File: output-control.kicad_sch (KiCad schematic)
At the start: 57 parts, among them U18 ADS7828, U19 TCA9534PWR, U20 ADS7828

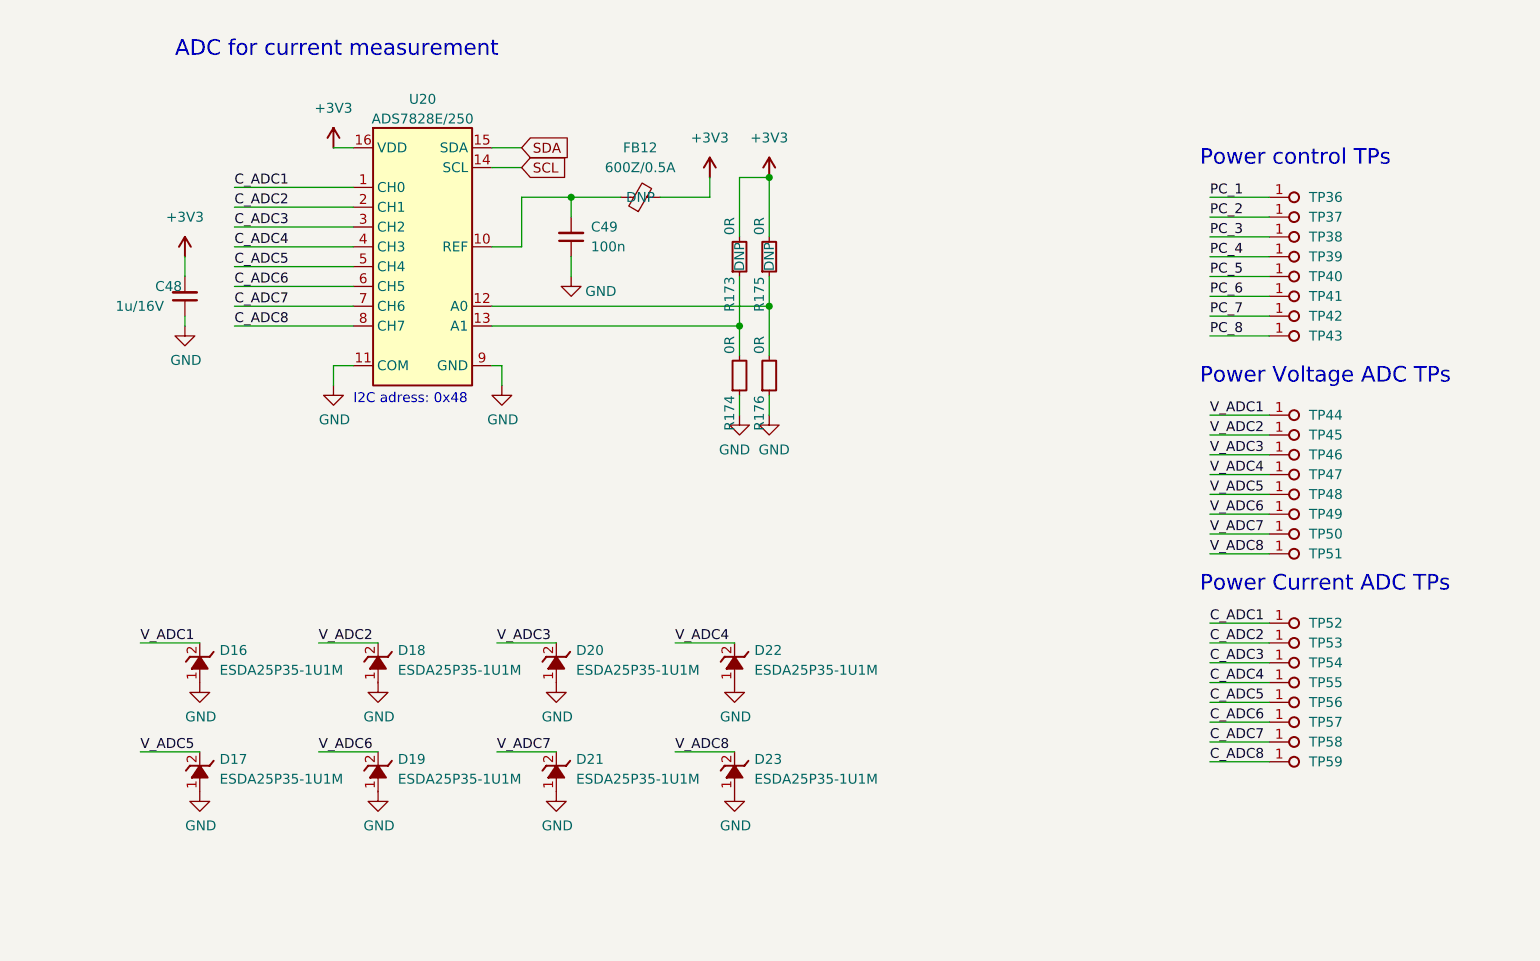
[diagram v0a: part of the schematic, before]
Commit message: Move testpoints to hierarchical sheets
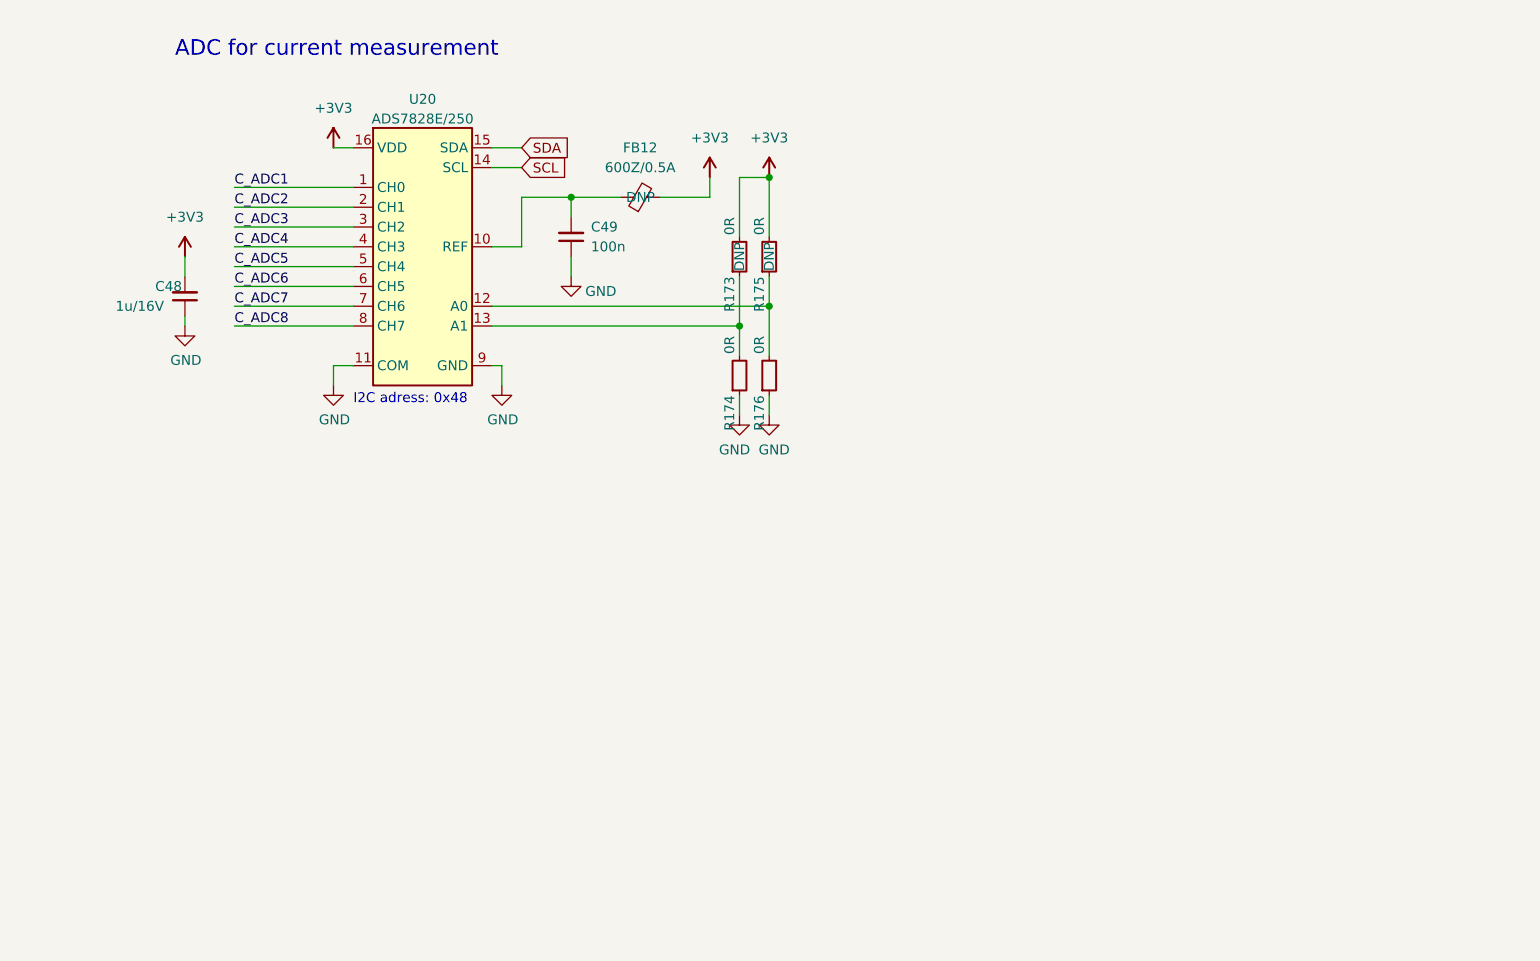
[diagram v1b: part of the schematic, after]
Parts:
- removed D16, D17, D18, D19, D20, D21, D22, D23: ESDA25P35-1U1M, antmicro-footprints:ESDA25P35-1U1M, symbol antmicroTVSDiodes:ESDA25P35-1U1M
- removed TP36, TP37, TP38, TP39, TP40, TP41, TP42, TP43, TP44, TP45, TP46, TP47, TP48, TP49, TP50, TP51, TP52, TP53, TP54, TP55, TP56, TP57, TP58, TP59: TP_1mm_SMD, antmicro-footprints:TP_SMD_1mm, symbol antmicroTestPoints:TP_1mm_SMD
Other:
- note removed: "Power Current ADC TPs"
- note removed: "Power Voltage ADC TPs"
- note removed: "Power control TPs"

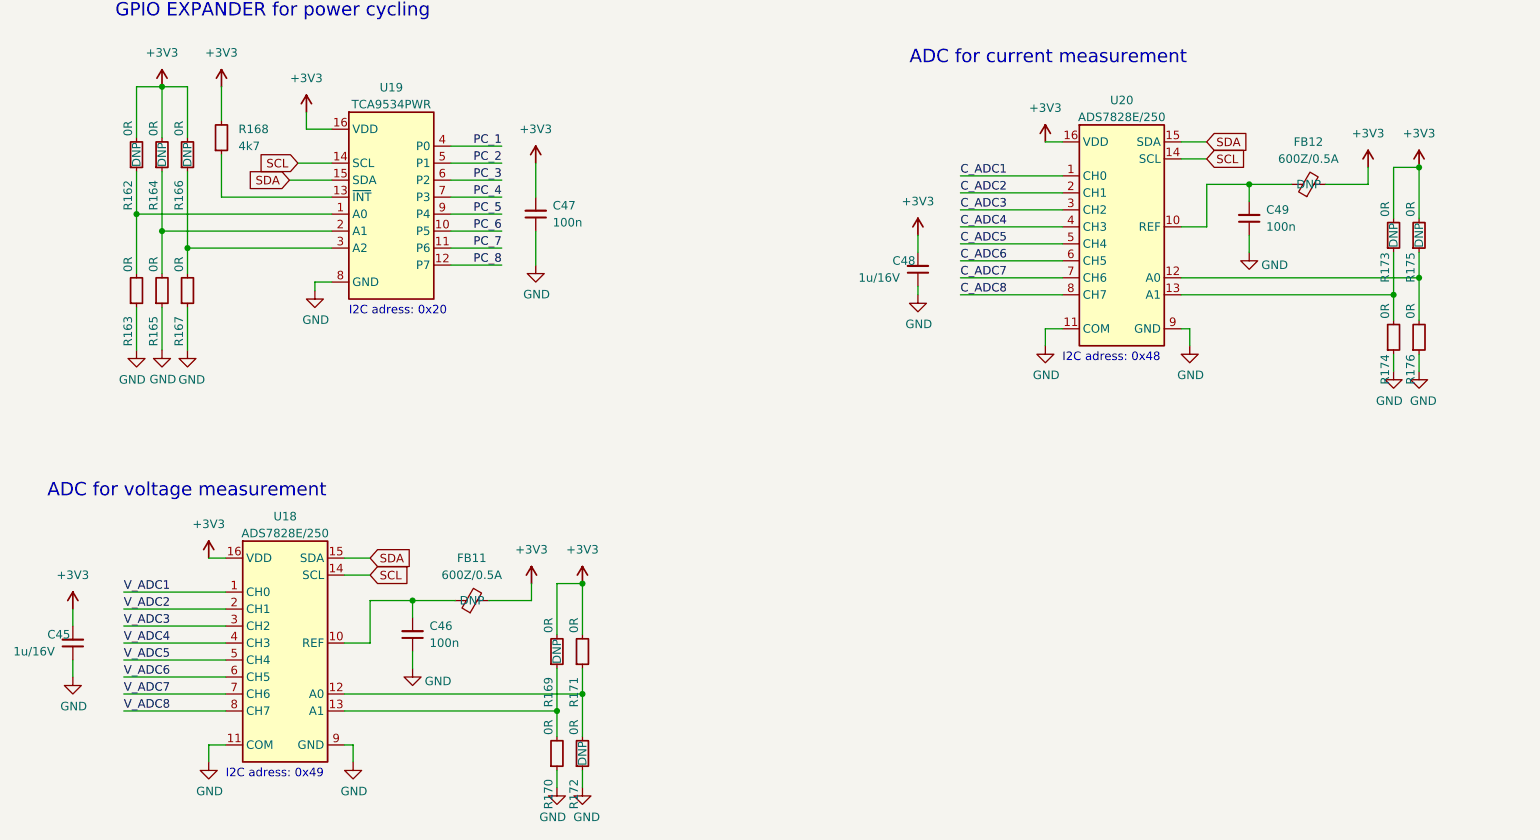
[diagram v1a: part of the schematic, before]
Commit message: Placement of supply section on PCB
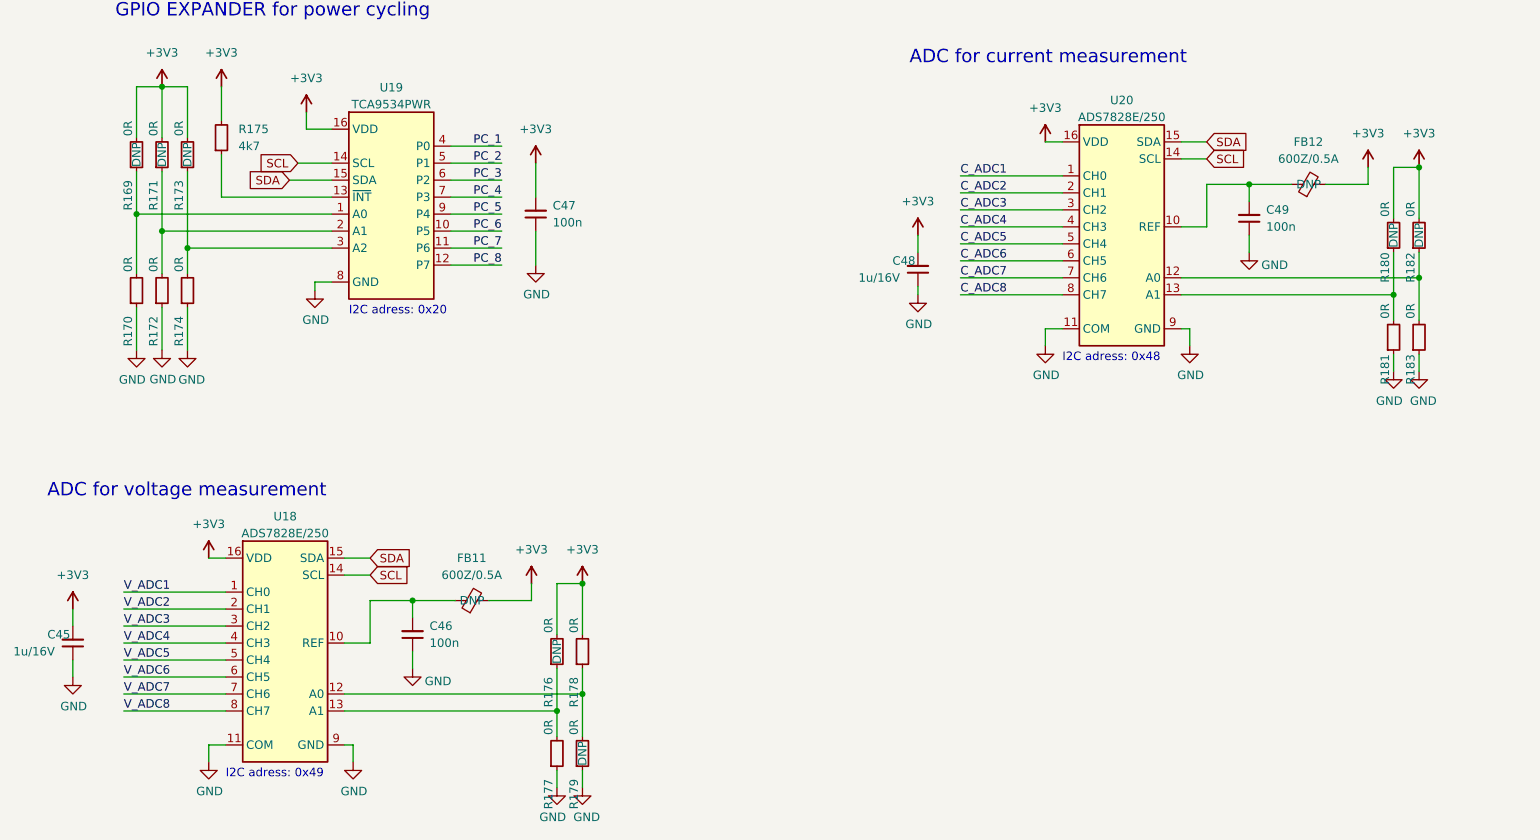
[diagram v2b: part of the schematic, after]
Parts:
- renumbered R162 to R169, R163 to R170, R164 to R171, R165 to R172, R166 to R173, R167 to R174, R168 to R175, R169 to R176, R170 to R177, R171 to R178, R172 to R179, R173 to R180, R174 to R181, R175 to R182, R176 to R183

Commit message: Implement changes suggested in schematic review
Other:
- company: (none) -> Antmicro Ltd
- moved on the sheet: C45, C46, C47, C48, C49, FB11, FB12, R169, R170, R171, R172, R173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

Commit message: 2nd part of review changes
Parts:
- added C61, C66: C_100n_0402, antmicro-footprints:C_0402_1005Metric, symbol antmicroCapacitors0402:C_100n_0402
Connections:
- net +3V3: now also C61.2, C66.2
- net GND: now also C61.1, C66.1
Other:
- moved on the sheet: C45, C46, C48, C49, FB11, FB12, R176, R177, R178, R179, R180, R181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

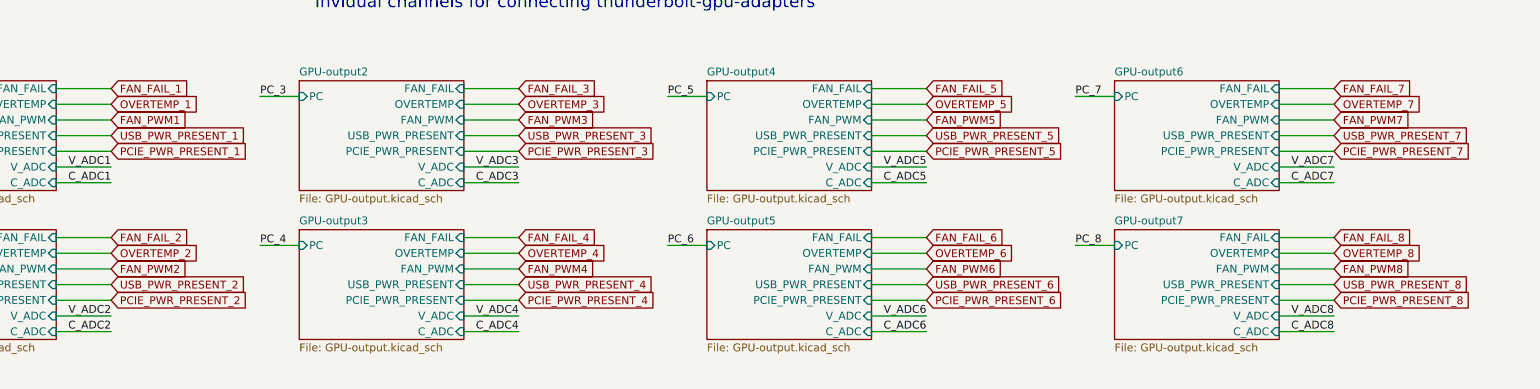
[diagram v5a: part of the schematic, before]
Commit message: Fix possible ERC errors
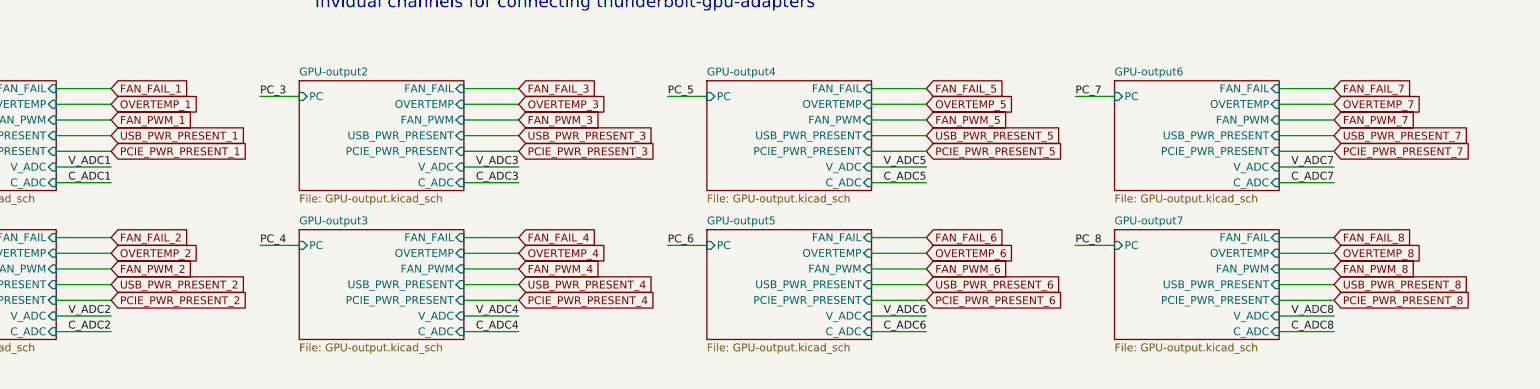
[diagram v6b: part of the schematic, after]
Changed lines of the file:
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@@
     )
   )
-  (global_label "FAN_PWM4" (shape input) (at 191.77 93.98 0) (fields_autoplaced)
-    (effects (font (size 1.27 1.27)) (justify left))
-    (property "Intersheet References" "${INTERSHEET_REFS}" (id 0) (at 203.9518 93.9006 0)
-      (effects (font (size 1.27 1.27)) (justify left) hide)
-    )
-  )
-  (global_label "FAN_PWM7" (shape input) (at 323.85 69.85 0) (fields_autoplaced)
-    (effects (font (size 1.27 1.27)) (justify left))
-    (property "Intersheet References" "${INTERSHEET_REFS}" (id 0) (at 336.0318 69.7706 0)
-      (effects (font (size 1.27 1.27)) (justify left) hide)
-    )
-  )
-  (global_label "FAN_PWM2" (shape input) (at 125.73 93.98 0) (fields_autoplaced)
-    (effects (font (size 1.27 1.27)) (justify left))
-    (property "Intersheet References" "${INTERSHEET_REFS}" (id 0) (at 137.9118 93.9006 0)
+  (global_label "FAN_PWM_4" (shape input) (at 191.77 93.98 0) (fields_autoplaced)
+    (effects (font (size 1.27 1.27)) (justify left))
+    (property "Intersheet References" "${INTERSHEET_REFS}" (id 0) (at 204.9194 93.9006 0)
+      (effects (font (size 1.27 1.27)) (justify left) hide)
+    )
+  )
+  (global_label "FAN_PWM_7" (shape input) (at 323.85 69.85 0) (fields_autoplaced)
+    (effects (font (size 1.27 1.27)) (justify left))
+    (property "Intersheet References" "${INTERSHEET_REFS}" (id 0) (at 336.9994 69.7706 0)
+      (effects (font (size 1.27 1.27)) (justify left) hide)
+    )
+  )
+  (global_label "FAN_PWM_2" (shape input) (at 125.73 93.98 0) (fields_autoplaced)
+    (effects (font (size 1.27 1.27)) (justify left))
+    (property "Intersheet References" "${INTERSHEET_REFS}" (id 0) (at 138.8794 93.9006 0)
       (effects (font (size 1.27 1.27)) (justify left) hide)
     )
@@
     )
   )
-  (global_label "FAN_PWM8" (shape input) (at 323.85 93.98 0) (fields_autoplaced)
-    (effects (font (size 1.27 1.27)) (justify left))
-    (property "Intersheet References" "${INTERSHEET_REFS}" (id 0) (at 336.0318 93.9006 0)
+  (global_label "FAN_PWM_8" (shape input) (at 323.85 93.98 0) (fields_autoplaced)
+    (effects (font (size 1.27 1.27)) (justify left))
+    (property "Intersheet References" "${INTERSHEET_REFS}" (id 0) (at 336.9994 93.9006 0)
       (effects (font (size 1.27 1.27)) (justify left) hide)
     )
@@
     )
   )
-  (global_label "FAN_PWM1" (shape input) (at 125.73 69.85 0) (fields_autoplaced)
-    (effects (font (size 1.27 1.27)) (justify left))
-    (property "Intersheet References" "${INTERSHEET_REFS}" (id 0) (at 137.9118 69.7706 0)
+  (global_label "FAN_PWM_1" (shape input) (at 125.73 69.85 0) (fields_autoplaced)
+    (effects (font (size 1.27 1.27)) (justify left))
+    (property "Intersheet References" "${INTERSHEET_REFS}" (id 0) (at 138.8794 69.7706 0)
       (effects (font (size 1.27 1.27)) (justify left) hide)
     )
@@
     )
   )
-  (global_label "FAN_PWM6" (shape input) (at 257.81 93.98 0) (fields_autoplaced)
-    (effects (font (size 1.27 1.27)) (justify left))
-    (property "Intersheet References" "${INTERSHEET_REFS}" (id 0) (at 269.9918 93.9006 0)
+  (global_label "FAN_PWM_6" (shape input) (at 257.81 93.98 0) (fields_autoplaced)
+    (effects (font (size 1.27 1.27)) (justify left))
+    (property "Intersheet References" "${INTERSHEET_REFS}" (id 0) (at 270.9594 93.9006 0)
       (effects (font (size 1.27 1.27)) (justify left) hide)
     )
@@
     )
   )
-  (global_label "FAN_PWM3" (shape input) (at 191.77 69.85 0) (fields_autoplaced)
-    (effects (font (size 1.27 1.27)) (justify left))
-    (property "Intersheet References" "${INTERSHEET_REFS}" (id 0) (at 203.9518 69.7706 0)
+  (global_label "FAN_PWM_3" (shape input) (at 191.77 69.85 0) (fields_autoplaced)
+    (effects (font (size 1.27 1.27)) (justify left))
+    (property "Intersheet References" "${INTERSHEET_REFS}" (id 0) (at 204.9194 69.7706 0)
       (effects (font (size 1.27 1.27)) (justify left) hide)
     )
@@
     )
   )
-  (global_label "FAN_PWM5" (shape input) (at 257.81 69.85 0) (fields_autoplaced)
-    (effects (font (size 1.27 1.27)) (justify left))
-    (property "Intersheet References" "${INTERSHEET_REFS}" (id 0) (at 269.9918 69.7706 0)
-      (effects (font (size 1.27 1.27)) (justify left) hide)
-    )
+  (global_label "FAN_PWM_5" (shape input) (at 257.81 69.85 0) (fields_autoplaced)
+    (effects (font (size 1.27 1.27)) (justify left))
+    (property "Intersheet References" "${INTERSHEET_REFS}" (id 0) (at 270.9594 69.7706 0)
+      (effects (font (size 1.27 1.27)) (justify left) hide)
+    )
